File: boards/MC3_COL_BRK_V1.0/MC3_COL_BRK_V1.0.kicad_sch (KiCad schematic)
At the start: 18 parts, among them J1 HARNESS_FFC_6P, J2 PWR_IN, J3 PWR_OUT, J4 CAN_IN, J5 CAN_OUT, J6 YAW_MOTOR, SW1 CAN_TERM

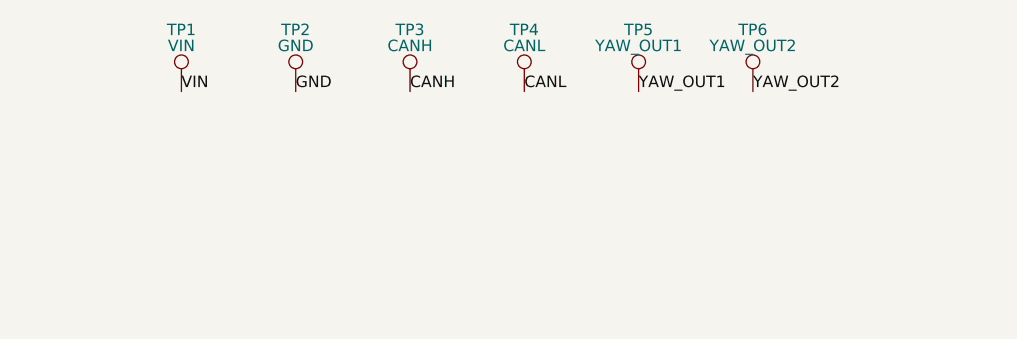
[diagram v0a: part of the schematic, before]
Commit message: MC3_COL_BRK: drop test points — every net is probeable on THT XH pins; ERC clean
Co-Authored-By: Claude Fable 5 <noreply@anthropic.com>
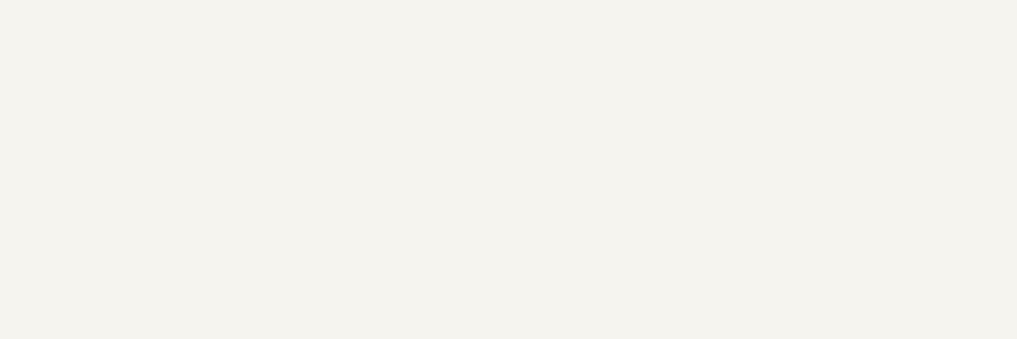
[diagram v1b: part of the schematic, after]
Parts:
- removed TP1: VIN, MC3_COL_BRK:TestPoint_Pad_1.0x1.0mm, symbol Connector:TestPoint
- removed TP2: GND, MC3_COL_BRK:TestPoint_Pad_1.0x1.0mm, symbol Connector:TestPoint
- removed TP3: CANH, MC3_COL_BRK:TestPoint_Pad_1.0x1.0mm, symbol Connector:TestPoint
- removed TP4: CANL, MC3_COL_BRK:TestPoint_Pad_1.0x1.0mm, symbol Connector:TestPoint
- removed TP5: YAW_OUT1, MC3_COL_BRK:TestPoint_Pad_1.0x1.0mm, symbol Connector:TestPoint
- removed TP6: YAW_OUT2, MC3_COL_BRK:TestPoint_Pad_1.0x1.0mm, symbol Connector:TestPoint

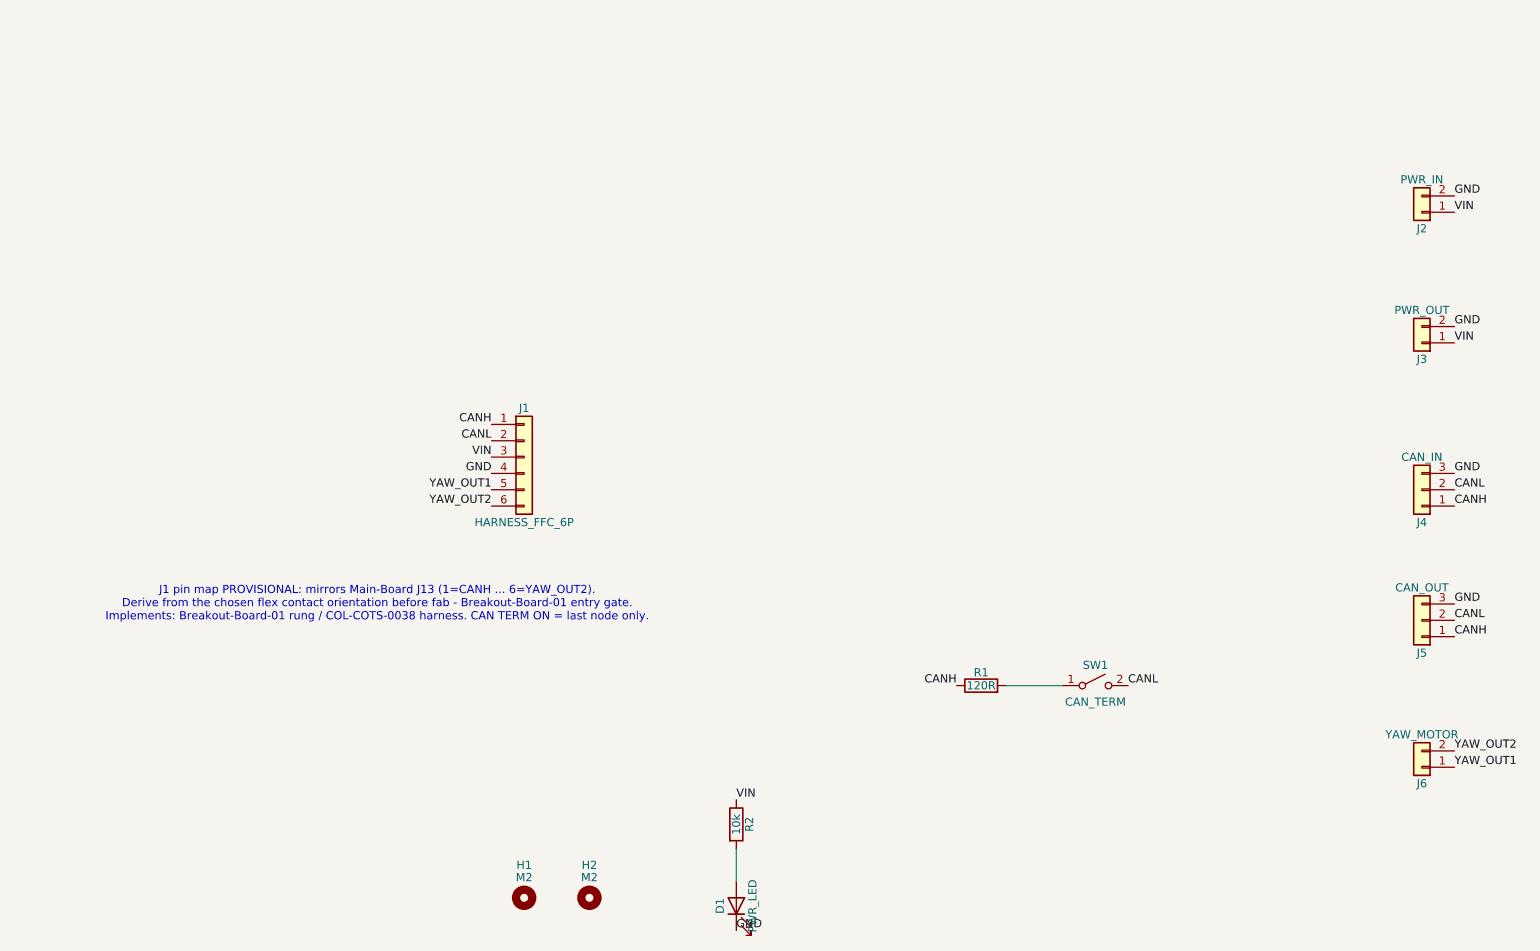
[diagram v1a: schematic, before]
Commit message: MC3_COL_BRK: FFC rear courtyard/silk walked back for edge-overhang mounting; H3 third M2 hole added
Co-Authored-By: Claude Fable 5 <noreply@anthropic.com>
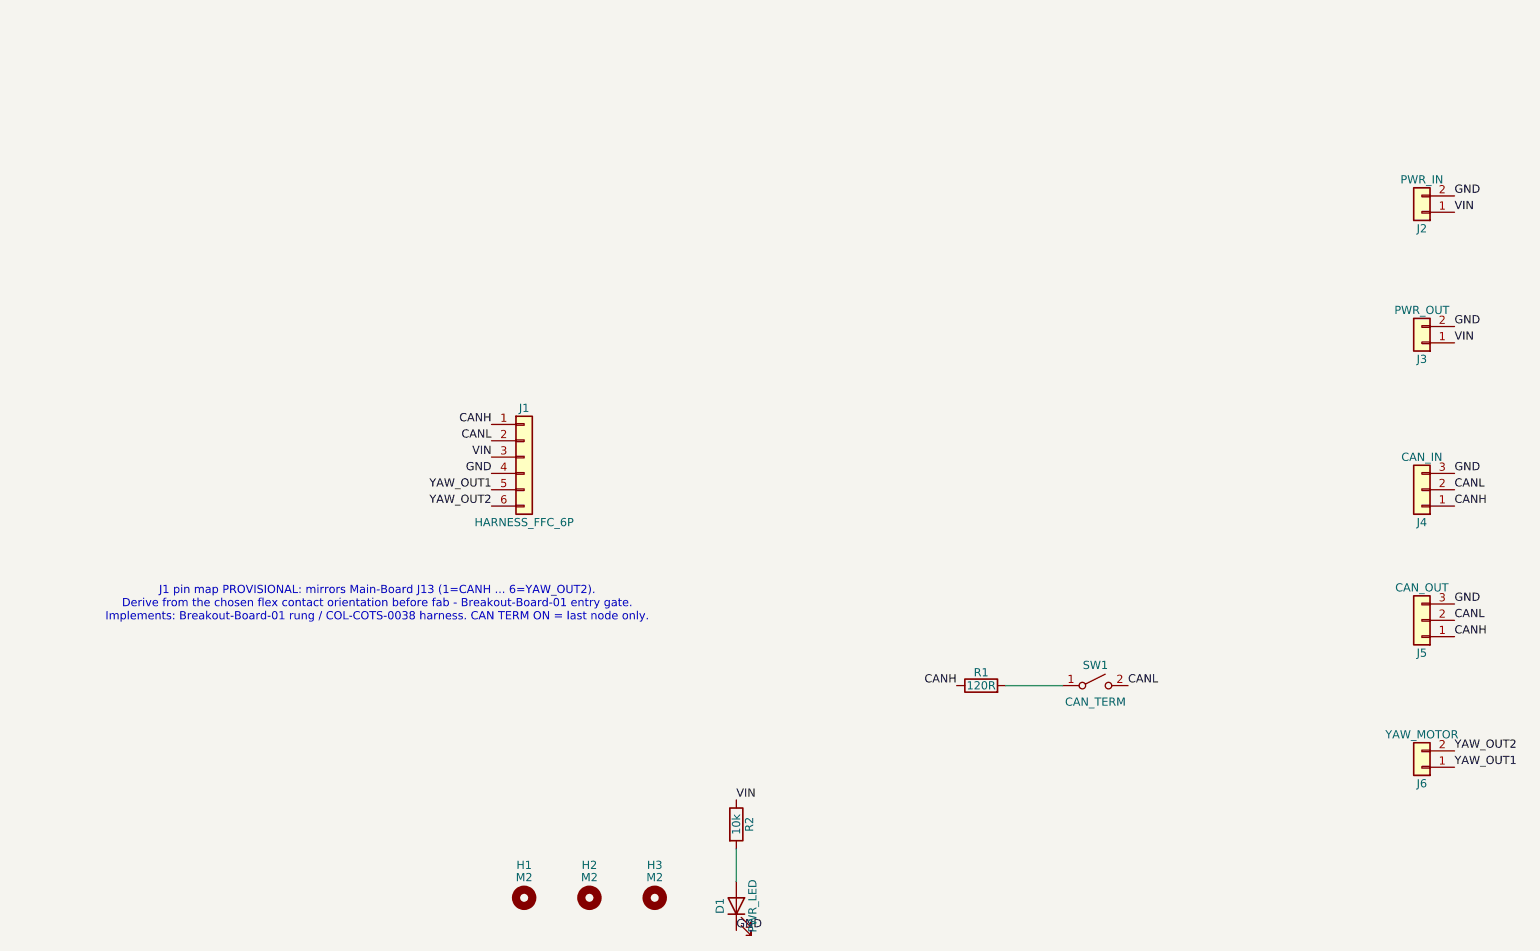
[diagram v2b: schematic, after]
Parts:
- added H3: M2, MC3_COL_BRK:MountingHole_2.2mm_M2, symbol Mechanical:MountingHole
